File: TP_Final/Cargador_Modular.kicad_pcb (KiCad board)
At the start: 2 copper layers, 198.1 x 99.7 mm, 180 parts, among them J101 BG 1x2, J102 BG 1x2, J103 BG 1x2, J104 BG 1x3, J105 Pin Header1x4, J106 Pin socket 2x4, J107 Pin Header 2x3, J108 BG2, J109 2 x BG2, J110 BG2, J111 Conector pol. 1x3, J112 BG2, J113 Conector pol. 1x3, J114 Conector pol. 1x3, J115 BG2, J116 BG2, K101 2FORM-C 2A 12VCC, K102 2FORM-C 2A 12VCC, K103 2FORM-C 2A 12VCC, K104 2FORM-C 2A 12VCC, Q101 2N3904, Q102 2N3904, Q103 2N3904, Q104 2N3904, Q105 2N3904, Q106 2N3904, Q107 2N3904, Q108 2N3904, Q109 2N3904, Q110 2N3904, SW101 SW_Push, SW102 KS01-B, SW103 KS01-B, SW104 KS01-B, SW105 KS01-B, U101 LM35-ZD, U102 STM32F103RBTx, U103 24LC256, U104 OP07, U105 OP07, U106 OP07, U107 LM7805_TO220, U108 LD1117S33TR_SOT223, Y101 8Mhz, Y102 32.768Khz

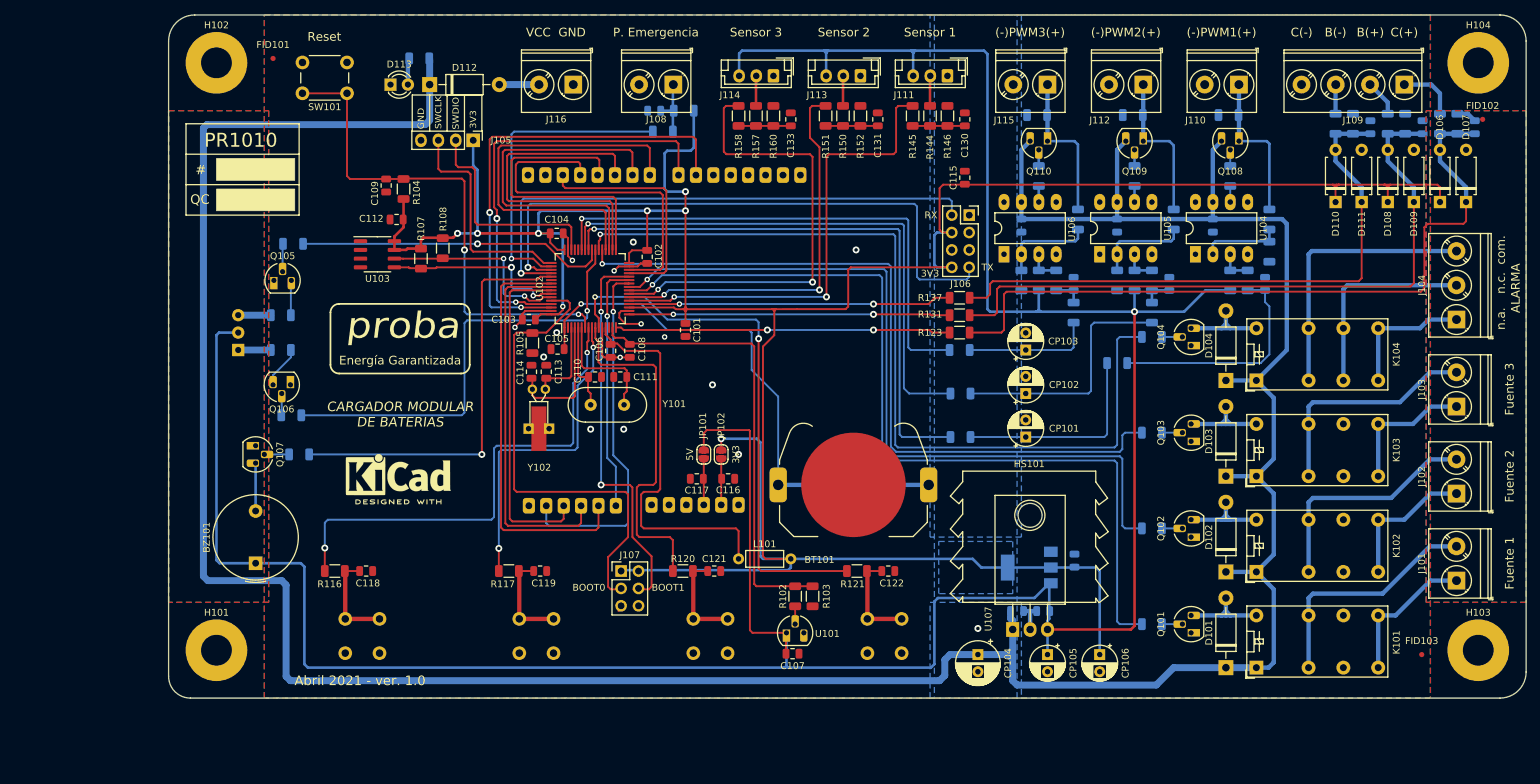
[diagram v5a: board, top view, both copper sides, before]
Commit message: Se finaliza el diseño del PCB
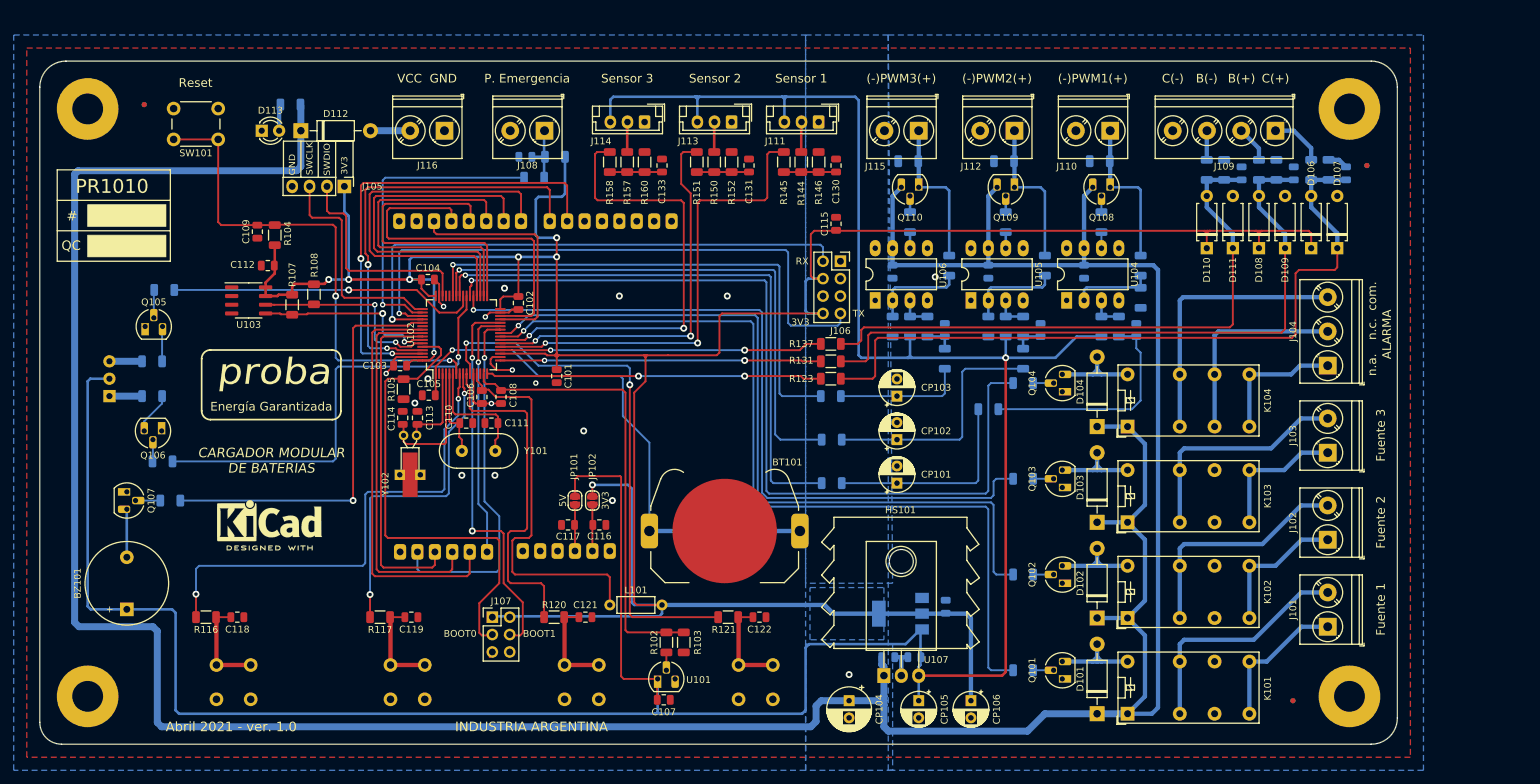
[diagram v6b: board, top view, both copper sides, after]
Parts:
- added FID104: Fiducial, Fiducial:Fiducial_0.75mm_Mask1.5mm, B.Cu at (52.3, 48.6)
- added FID105: Fiducial, Fiducial:Fiducial_0.75mm_Mask1.5mm, B.Cu at (230.8, 57.5)
- added FID106: Fiducial, Fiducial:Fiducial_0.75mm_Mask1.5mm, B.Cu at (220.0, 135.6)
- BZ101: footprint Buzzer_Beeper:Buzzer_TDK_PS1240P02BT_D12.2mm_H6.5mm -> Buzzer_Beeper:Buzzer_12x9.5RM7.6
- moved BZ101 20.4 mm to (49.8, 122.3)
- moved C115 20.0 mm to (153.3, 66.0)
- moved C129 20.0 mm to (183.1, 81.5)
- moved C134 20.0 mm to (169.2, 81.5)
- moved JP101 20.0 mm to (115.2, 106.4)
- moved R137 20.0 mm to (152.5, 83.6)
- moved R154 20.0 mm to (152.5, 91.2)
- moved BT101 20.0 mm to (137.0, 110.9)
- moved C130 20.0 mm to (153.3, 57.5)
- moved C135 20.0 mm to (160.9, 129.3)
- moved CP104 20.0 mm to (155.2, 135.6)
- moved CP106 20.0 mm to (173.0, 135.6)
- moved D110 20.0 mm to (207.4, 69.6)
- moved D111 20.0 mm to (211.2, 69.6)
- moved R103 20.0 mm to (131.1, 127.1)
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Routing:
- net +12V: track 453.9 -> 496.9 mm
- net Net-(J109-Pad1): track 8.72 -> 7.97 mm
- net GNDA: vias 15 -> 17
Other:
- board text added: "Cargador modular de baterías Modelo: PR1010"
- board text added: "Errores aprobados: Superposición de huella entre regulador 7805 (U107) y disipador (HS101)"
- board text added: "INDUSTRIA ARGENTINA"
- board text added: "Terminación superficial : HASL Espesor final aprox. :1.6mm Material: FR4 Grillas usadas: 25mils, 5mils, 0.5mils Trazos usados: 40mils, 25mils, 15mils y 11mils Vías usadas: 31.5/15.7 mils y 40/20mils Separación mínima entre trazas: 7mils / 0.18mm Distancia de cobre a borde: 20mils / 0.5mm"
